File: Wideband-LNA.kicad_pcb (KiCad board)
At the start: 4 copper layers, 18.8 x 18.8 mm, 28 parts, among them J1 RF-IN, J2 RF-OUT, J3 USB_C_Receptacle_USB2.0_16P, U1 TQP3M9036, U2 AP2127K-ADJ

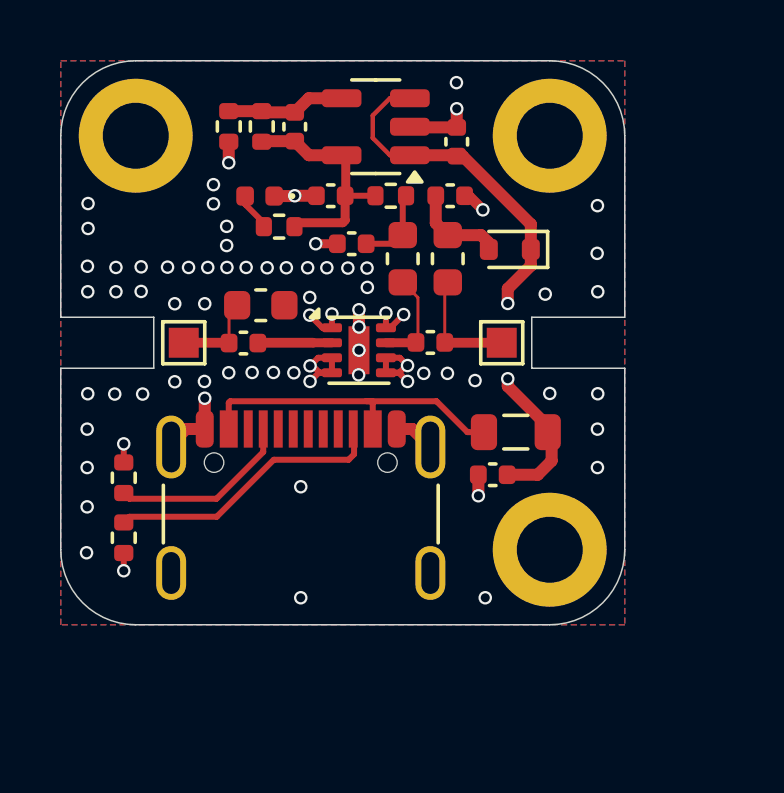
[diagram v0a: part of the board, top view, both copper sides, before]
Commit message: Add zone mask to relieve ground plane under component pads
Added screen shot of JLCPCB impedance calculator
Removed bias T components
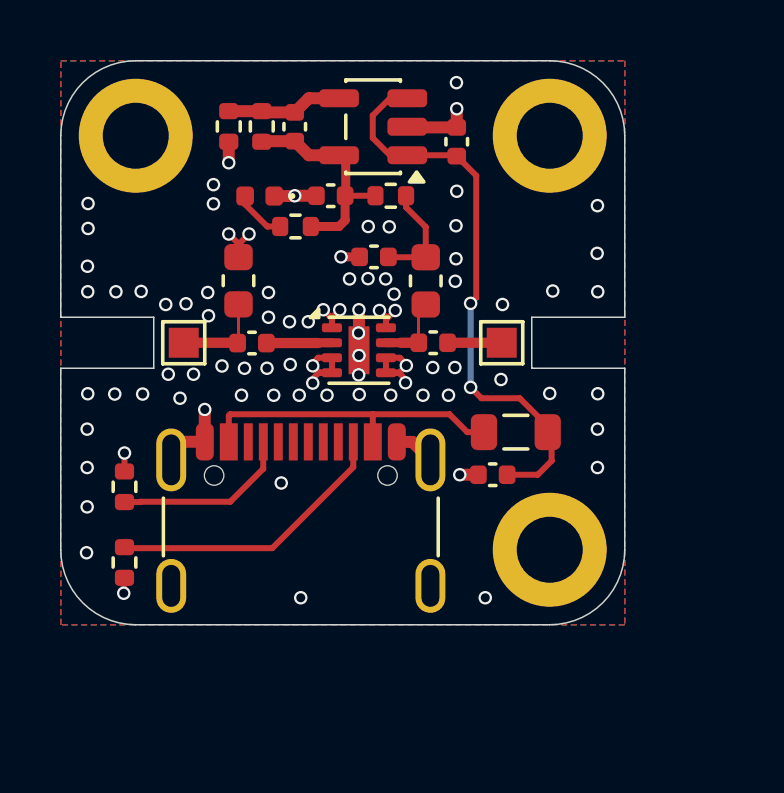
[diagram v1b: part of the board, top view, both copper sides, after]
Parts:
- removed C8: 330p, Capacitor_SMD:C_0402_1005Metric
- removed D2: D, Diode_SMD:D_SOD-523
- removed L3: 680n, Inductor_SMD:L_0603_1608Metric
- moved L5 1.10 mm to (106.5, 97.9), turned to 90 degrees
- moved L2 1.06 mm to (112.8, 97.9)
- moved C3 0.86 mm to (111.0, 97.1)
- moved R4 0.83 mm to (102.7, 107.3)
- moved R2 0.55 mm to (108.4, 96.1)
- moved J3 0.43 mm to (108.6, 107.0)
- moved R3 0.30 mm to (102.7, 104.8)
- moved C2 0.28 mm to (107.0, 100.0)
- moved C1 0.10 mm to (113.0, 100.0)
- moved U2 0.09 mm to (111.0, 92.8)
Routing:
- net Net-(D2-A): track 3.17 -> 0.00 mm
- net Net-(C1-Pad2): track 3.95 -> 1.81 mm
- net GND: track 21.0 -> 22.3 mm, vias 76 -> 86
- net Net-(C3-Pad1): track 2.70 -> 3.57 mm
- net Net-(U1-RFOUT): track 3.24 -> 2.47 mm
- net /4V8: track 7.96 -> 7.28 mm
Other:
- board text added: "LNA 50M-2G V3.4 (c) wa1hco 2025 Creative Commons License V4 Attribute and Share Alike"
- board text removed: "LNA 50-2000 MHz V3.4 (c) wa1hco 250219 Creative Commons License V4 Attribute and Share Alike"

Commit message: Preparing for fab and assy
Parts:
- removed D1: Emerald, Diode_SMD:D_0402_1005Metric
- removed R2: 1K, Resistor_SMD:R_0402_1005Metric
- moved C3 0.70 mm to (111.5, 97.6), turned to -90 degrees
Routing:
- net /4V8: track 7.28 -> 5.23 mm
- net Net-(D1-A): track 1.75 -> 0.00 mm
- net GND: track 22.3 -> 21.0 mm, vias 86 -> 84

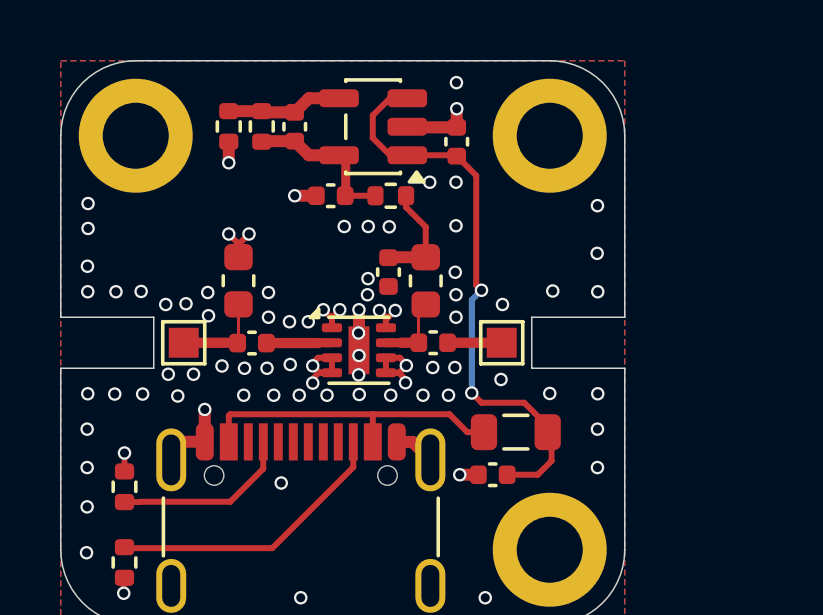
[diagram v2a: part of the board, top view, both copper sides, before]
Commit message: Added attenuator with high frequency bypass on output
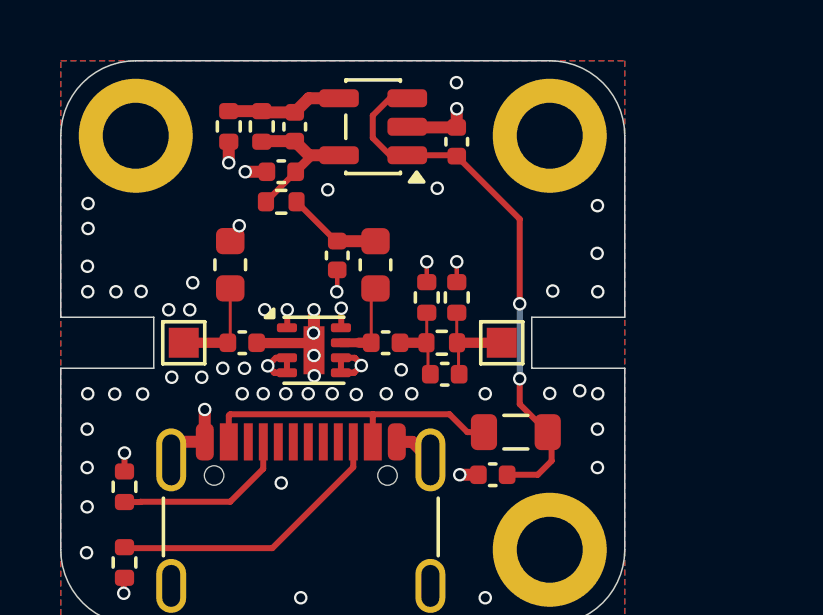
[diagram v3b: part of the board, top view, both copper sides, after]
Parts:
- added C8: 10p, Capacitor_SMD:C_0402_1005Metric, F.Cu at (113.4, 101.0)
- added R2: 10, Resistor_SMD:R_0402_1005Metric, F.Cu at (112.8, 98.5)
- added R7: 10, Resistor_SMD:R_0402_1005Metric, F.Cu at (113.8, 98.5)
- added R8: 10, Resistor_SMD:R_0402_1005Metric, F.Cu at (113.3, 100.0)
- C1, C2, C3: value 330p -> 1nF
- moved R1 3.66 mm to (108.0, 95.3)
- moved C4 1.83 mm to (108.0, 94.3)
- moved C3 1.80 mm to (109.8, 97.1)
- moved L2 1.76 mm to (111.1, 97.4)
- moved C1 1.58 mm to (111.4, 100.0)
- moved U1 1.50 mm to (109.0, 100.2)
- moved L5 0.60 mm to (106.2, 97.4)
- moved C2 0.33 mm to (106.7, 100.0)
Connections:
- J2 pad 1: Net-(C1-Pad2) -> Net-(C8-Pad2)
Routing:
- net Net-(C8-Pad2): track 0.00 -> 3.52 mm
- net GND: track 21.0 -> 19.5 mm, vias 84 -> 65
- net Net-(C1-Pad2): track 1.81 -> 2.91 mm
- net /5V: track 19.4 -> 18.4 mm
- net Net-(U1-RFOUT): track 2.47 -> 3.21 mm
- net /4V8: track 5.23 -> 5.86 mm

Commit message: Updated jlcpcb components
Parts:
- C1, C2, C3: value 1nF -> 330p
- L2, L5: value 680n -> 470n
- R2, R7: value 10 -> 105
- R8: value 10 -> 61.9
- U1: value TQP3M9036 -> TQP3M9037
- moved C4 4.85 mm to (112.7, 95.4), turned to 0 degrees
- moved R1 3.31 mm to (111.2, 95.5), turned to -90 degrees
- moved L5 0.89 mm to (105.5, 97.9), turned to 180 degrees
- moved C3 0.59 mm to (110.0, 97.7)
- moved L2 0.57 mm to (111.2, 98.0)
- moved C8 0.08 mm to (113.3, 101.0)
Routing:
- net Net-(U1-RFIN): track 2.49 -> 1.10 mm
- net Net-(U1-RFOUT): track 3.21 -> 2.29 mm
- net Net-(C3-Pad1): track 3.18 -> 2.41 mm
- net GND: vias 65 -> 77
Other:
- board text added: "LNA 50M-3GHz V3.4 (c) wa1hco 2025 Creative Commons License V4 Attribute and Share Alike"
- board text removed: "LNA 50M-2G V3.4 (c) wa1hco 2025 Creative Commons License V4 Attribute and Share Alike"
